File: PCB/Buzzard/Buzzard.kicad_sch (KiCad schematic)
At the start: 87 parts, among them J1 PJ-320A, J2 LCD, J4 Haptic Buzz, J5 TrackPoint, J6 OLED, J8 Battery, SW1 SW_DPST_x2, SW2 Reset, U1 ProMicro, U10 Hole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

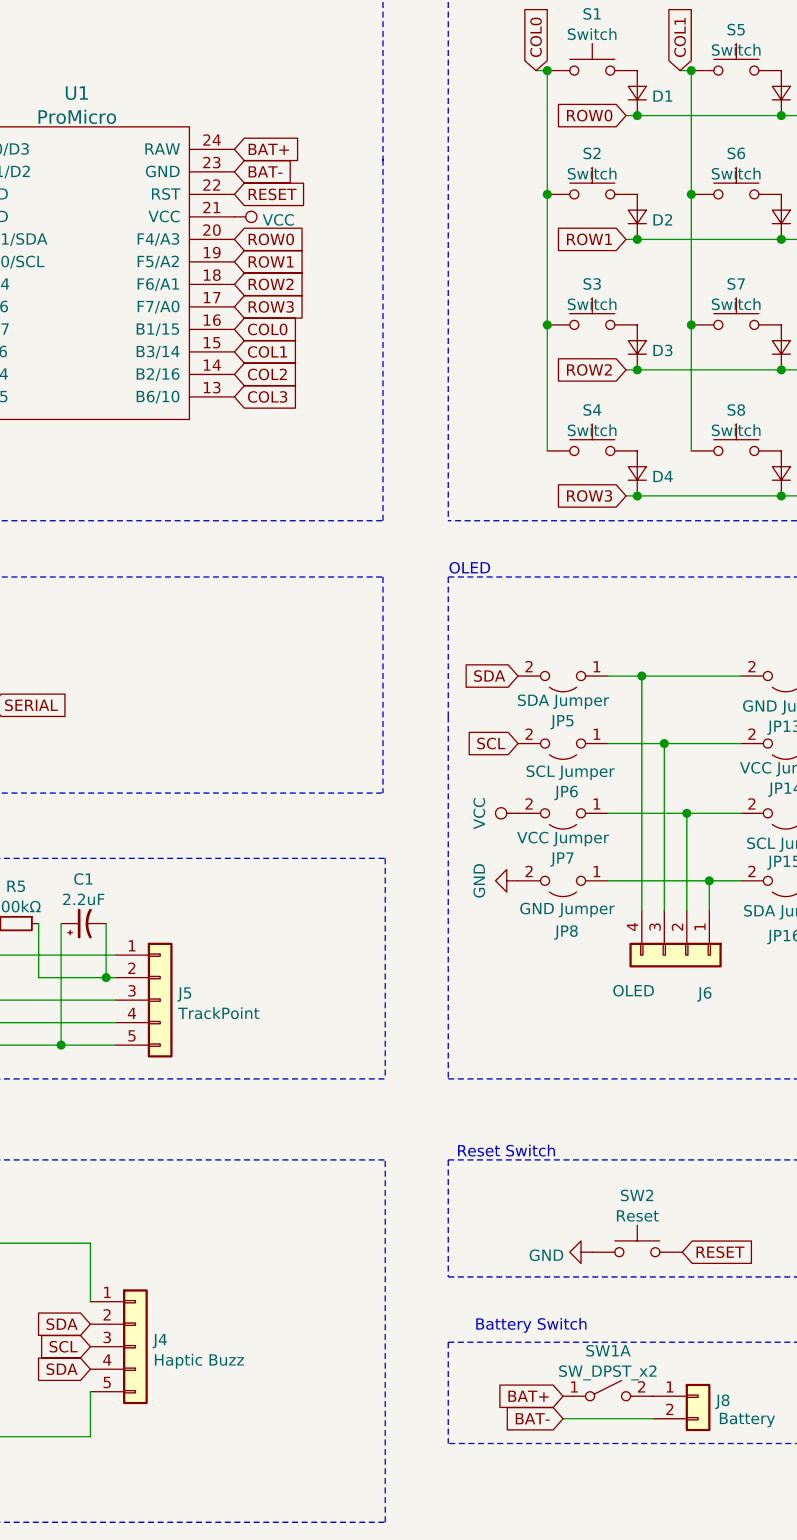
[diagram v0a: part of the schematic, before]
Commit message: rounded edge cuts
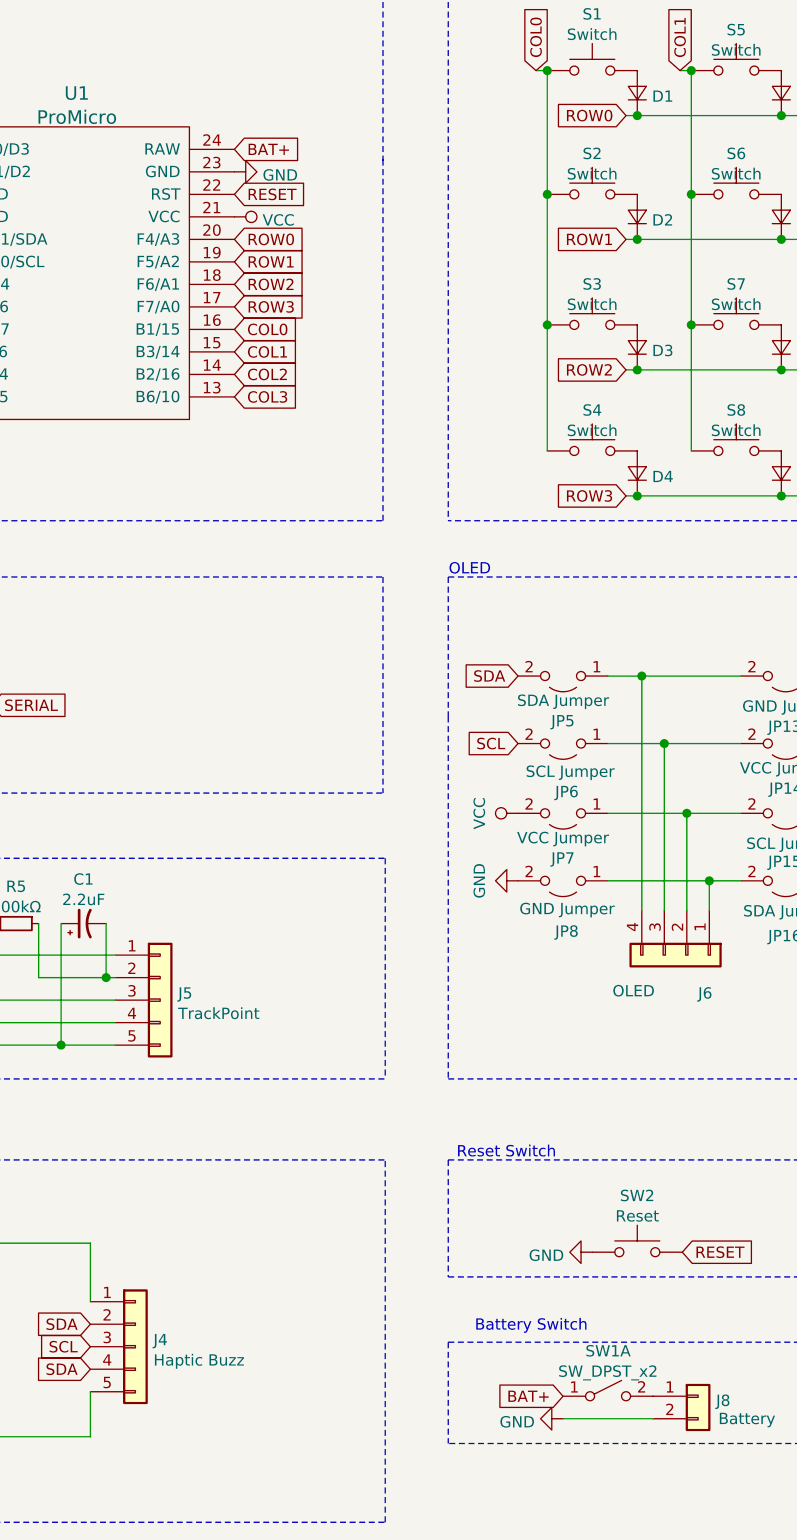
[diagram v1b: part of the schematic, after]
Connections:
- net BAT- is gone; now on net GND: J8.2 (Pin_2), U1.23 (GND)
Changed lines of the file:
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@@
-    )
-  )
-  (global_label "BAT-" (shape input) (at 89.154 37.592 0) (fields_autoplaced)
-    (effects (font (size 1.27 1.27)) (justify left))
-    (property "Intersheet References" "${INTERSHEET_REFS}" (id 0) (at 96.4657 37.6714 0)
-      (effects (font (size 1.27 1.27)) (justify left) hide)
     )
   )
@@
     )
   )
-  (global_label "BAT-" (shape input) (at 126.238 178.308 180) (fields_autoplaced)
-    (effects (font (size 1.27 1.27)) (justify right))
-    (property "Intersheet References" "${INTERSHEET_REFS}" (id 0) (at 118.9263 178.2286 0)
-      (effects (font (size 1.27 1.27)) (justify right) hide)
-    )
-  )
   (global_label "ROW0" (shape input) (at 133.35 31.242 180) (fields_autoplaced)
     (effects (font (size 1.27 1.27)) (justify right))
@@
     (pin "1")
   )
+  (symbol (lib_id "power:GND") (at 89.154 37.592 90) (unit 1)
+    (in_bom yes) (on_board yes) (fields_autoplaced)
+    (property "Reference" "#PWR?" (id 0) (at 95.504 37.592 0)
+      (effects (font (size 1.27 1.27)) hide)
+    )
+    (property "Value" "GND" (id 1) (at 92.3291 37.9805 90)
+      (effects (font (size 1.27 1.27)) (justify right))
+    )
+    (property "Footprint" "" (id 2) (at 89.154 37.592 0)
+      (effects (font (size 1.27 1.27)) hide)
+    )
+    (property "Datasheet" "" (id 3) (at 89.154 37.592 0)
+      (effects (font (size 1.27 1.27)) hide)
+    )
+    (pin "1")
+  )
   (symbol (lib_id "power:GND") (at 121.158 117.602 270) (unit 1)
     (in_bom yes) (on_board yes) (fields_autoplaced)
@@
     )
     (property "Datasheet" "" (id 3) (at 121.158 117.602 0)
+      (effects (font (size 1.27 1.27)) hide)
+    )
+    (pin "1")
+  )
+  (symbol (lib_id "power:GND") (at 126.238 178.308 270) (unit 1)
+    (in_bom yes) (on_board yes) (fields_autoplaced)
+    (property "Reference" "#PWR?" (id 0) (at 119.888 178.308 0)
+      (effects (font (size 1.27 1.27)) hide)
+    )
+    (property "Value" "GND" (id 1) (at 123.063 178.6965 90)
+      (effects (font (size 1.27 1.27)) (justify right))
+    )
+    (property "Footprint" "" (id 2) (at 126.238 178.308 0)
+      (effects (font (size 1.27 1.27)) hide)
+    )
+    (property "Datasheet" "" (id 3) (at 126.238 178.308 0)
       (effects (font (size 1.27 1.27)) hide)
     )
@@
       (reference "#PWR021") (unit 1) (value "GND") (footprint "")
     )
+    (path "/24c49c4a-95c7-4ec6-bf5c-36e77974586a"
+      (reference "#PWR?") (unit 1) (value "GND") (footprint "")
+    )
+    (path "/4907b72c-e6f0-40ff-9e41-6ac4ee21b3ef"
+      (reference "#PWR?") (unit 1) (value "GND") (footprint "")
+    )
     (path "/c869f587-3433-4e49-b864-4e64391cc97e"

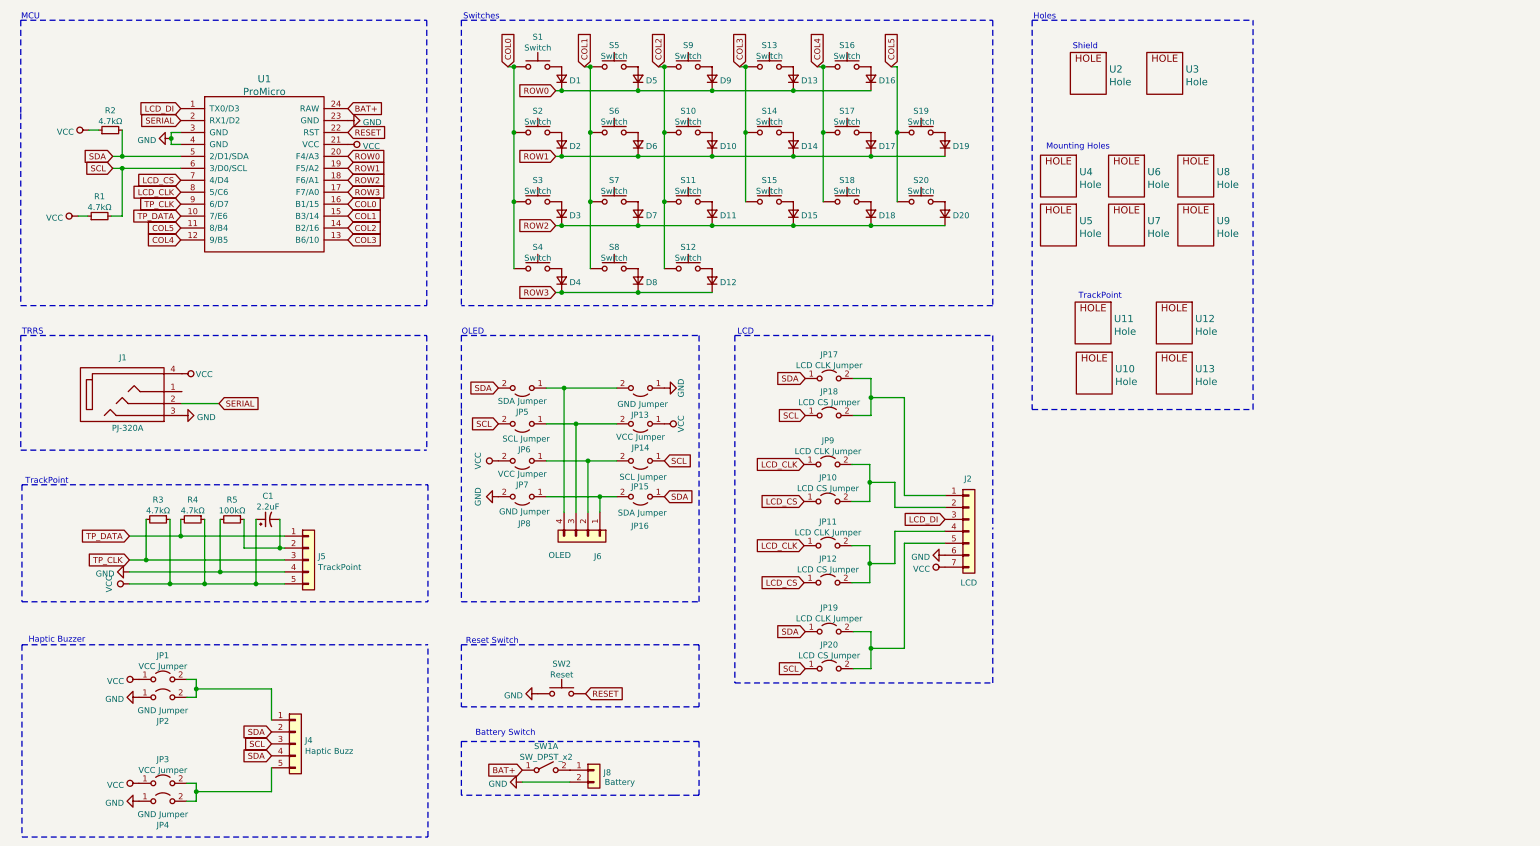
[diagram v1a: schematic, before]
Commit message: switched trrs lines and TP clock/data lines
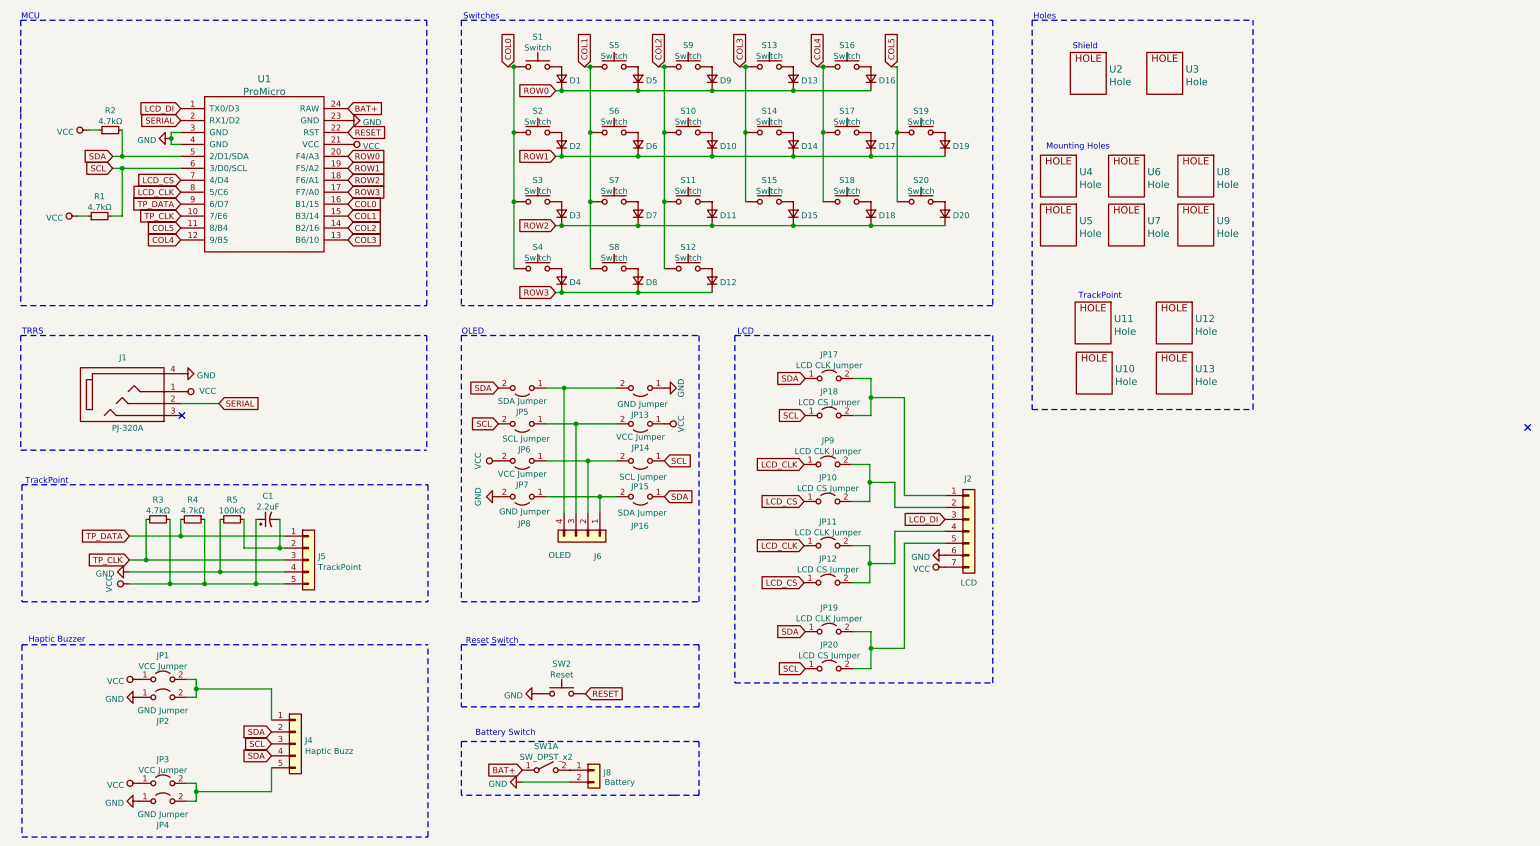
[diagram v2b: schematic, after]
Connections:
- net GND: now also J1.4; no longer J1.3
- net TP_CLK: now also U1.10 (7/E6); no longer U1.9 (6/D7)
- net TP_DATA: now also U1.9 (6/D7); no longer U1.10 (7/E6)
- net VCC: now also J1.1; no longer J1.4
- no-connect marks 0 -> 2
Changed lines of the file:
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@@
   (junction (at 200.406 149.86) (diameter 1.016) (color 0 0 0 0))
   (junction (at 205.994 40.132) (diameter 1.016) (color 0 0 0 0))
+  (no_connect (at 53.848 100.33))
+  (no_connect (at 340.106 102.87))
   (wire (pts (xy 31.75 57.912) (xy 33.782 57.912))
     (stroke (width 0) (type solid) (color 0 0 0 0))
@@
     )
   )
-  (global_label "TP_CLK" (shape input) (at 53.594 55.372 180) (fields_autoplaced)
-    (effects (font (size 1.27 1.27)) (justify right))
-    (property "Intersheet References" "${INTERSHEET_REFS}" (id 0) (at 44.4076 55.2926 0)
-      (effects (font (size 1.27 1.27)) (justify right) hide)
-    )
-  )
-  (global_label "TP_DATA" (shape input) (at 53.594 57.912 180) (fields_autoplaced)
-    (effects (font (size 1.27 1.27)) (justify right))
-    (property "Intersheet References" "${INTERSHEET_REFS}" (id 0) (at 43.5609 57.8326 0)
+  (global_label "TP_DATA" (shape input) (at 53.594 55.372 180) (fields_autoplaced)
+    (effects (font (size 1.27 1.27)) (justify right))
+    (property "Intersheet References" "${INTERSHEET_REFS}" (id 0) (at 43.5609 55.2926 0)
+      (effects (font (size 1.27 1.27)) (justify right) hide)
+    )
+  )
+  (global_label "TP_CLK" (shape input) (at 53.594 57.912 180) (fields_autoplaced)
+    (effects (font (size 1.27 1.27)) (justify right))
+    (property "Intersheet References" "${INTERSHEET_REFS}" (id 0) (at 44.4076 57.8326 0)
       (effects (font (size 1.27 1.27)) (justify right) hide)
     )
@@
     (pin "1")
   )
-  (symbol (lib_id "power:VCC") (at 53.848 91.44 270) (unit 1)
+  (symbol (lib_id "power:VCC") (at 53.848 95.25 270) (unit 1)
     (in_bom yes) (on_board yes)
-    (property "Reference" "#PWR09" (id 0) (at 50.038 91.44 0)
-      (effects (font (size 1.27 1.27)) hide)
-    )
-    (property "Value" "VCC" (id 1) (at 56.7691 91.5745 90)
+    (property "Reference" "#PWR09" (id 0) (at 50.038 95.25 0)
+      (effects (font (size 1.27 1.27)) hide)
+    )
+    (property "Value" "VCC" (id 1) (at 57.5311 95.1305 90)
       (effects (font (size 1.27 1.27)) (justify left))
     )
-    (property "Footprint" "" (id 2) (at 53.848 91.44 0)
-      (effects (font (size 1.27 1.27)) hide)
-    )
-    (property "Datasheet" "" (id 3) (at 53.848 91.44 0)
+    (property "Footprint" "" (id 2) (at 53.848 95.25 0)
+      (effects (font (size 1.27 1.27)) hide)
+    )
+    (property "Datasheet" "" (id 3) (at 53.848 95.25 0)
       (effects (font (size 1.27 1.27)) hide)
     )
@@
     (pin "1")
   )
-  (symbol (lib_id "power:GND") (at 53.848 100.33 90) (unit 1)
-    (in_bom yes) (on_board yes) (fields_autoplaced)
-    (property "Reference" "#PWR010" (id 0) (at 60.198 100.33 0)
-      (effects (font (size 1.27 1.27)) hide)
-    )
-    (property "Value" "GND" (id 1) (at 57.0231 100.7185 90)
+  (symbol (lib_id "power:GND") (at 53.848 91.44 90) (unit 1)
+    (in_bom yes) (on_board yes) (fields_autoplaced)
+    (property "Reference" "#PWR010" (id 0) (at 60.198 91.44 0)
+      (effects (font (size 1.27 1.27)) hide)
+    )
+    (property "Value" "GND" (id 1) (at 57.0231 91.8285 90)
       (effects (font (size 1.27 1.27)) (justify right))
     )
-    (property "Footprint" "" (id 2) (at 53.848 100.33 0)
-      (effects (font (size 1.27 1.27)) hide)
-    )
-    (property "Datasheet" "" (id 3) (at 53.848 100.33 0)
-      (effects (font (size 1.27 1.27)) hide)
-    )
+    (property "Footprint" "" (id 2) (at 53.848 91.44 0)
+      (effects (font (size 1.27 1.27)) hide)
+    )
+    (property "Datasheet" "" (id 3) (at 53.848 91.44 0)
+      (effects (font (size 1.27 1.27)) hide)
+    )

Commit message: Some fine tuning and silkmask improvments
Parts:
- JP17, JP19: value LCD CLK Jumper -> LCD EIN Jumper
- JP18, JP20: value LCD CS Jumper -> LCD DISP Jumper
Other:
- title: (none) -> Buzzard Split Keyboard
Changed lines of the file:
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@@
 (kicad_sch (version 20210406) (generator eeschema)
   (paper "A4")
+  (title_block
+    (title "Buzzard Split Keyboard")
+    (date "2021-11-13")
+    (rev "1")
+  )
   (junction (at 41.148 45.212) (diameter 1.016) (color 0 0 0 0))
   (junction (at 41.148 47.752) (diameter 1.016) (color 0 0 0 0))
@@
     (in_bom yes) (on_board yes) (fields_autoplaced)
     (property "Reference" "JP17" (id 0) (at 191.516 87.3718 0))
-    (property "Value" "LCD CLK Jumper" (id 1) (at 191.516 89.6705 0))
+    (property "Value" "LCD EIN Jumper" (id 1) (at 191.516 89.6705 0))
     (property "Footprint" "Jumper:SolderJumper-2_P1.3mm_Open_Pad1.0x1.5mm" (id 2) (at 191.516 92.456 0)
       (effects (font (size 1.27 1.27)) hide)
@@
     (in_bom yes) (on_board yes) (fields_autoplaced)
     (property "Reference" "JP18" (id 0) (at 191.516 95.2458 0))
-    (property "Value" "LCD CS Jumper" (id 1) (at 191.516 97.5445 0))
+    (property "Value" "LCD DISP Jumper" (id 1) (at 191.516 97.5445 0))
     (property "Footprint" "Jumper:SolderJumper-2_P1.3mm_Open_Pad1.0x1.5mm" (id 2) (at 191.516 100.33 0)
       (effects (font (size 1.27 1.27)) hide)
@@
     (in_bom yes) (on_board yes) (fields_autoplaced)
     (property "Reference" "JP19" (id 0) (at 191.516 141.2198 0))
-    (property "Value" "LCD CLK Jumper" (id 1) (at 191.516 143.5185 0))
+    (property "Value" "LCD EIN Jumper" (id 1) (at 191.516 143.5185 0))
     (property "Footprint" "Jumper:SolderJumper-2_P1.3mm_Open_Pad1.0x1.5mm" (id 2) (at 191.516 146.304 0)
       (effects (font (size 1.27 1.27)) hide)
@@
     (in_bom yes) (on_board yes) (fields_autoplaced)
     (property "Reference" "JP20" (id 0) (at 191.516 149.0938 0))
-    (property "Value" "LCD CS Jumper" (id 1) (at 191.516 151.3925 0))
+    (property "Value" "LCD DISP Jumper" (id 1) (at 191.516 151.3925 0))
     (property "Footprint" "Jumper:SolderJumper-2_P1.3mm_Open_Pad1.0x1.5mm" (id 2) (at 191.516 154.178 0)
       (effects (font (size 1.27 1.27)) hide)
@@
     )
     (path "/e7932f86-c33d-462c-8de4-76ea75a5e908"
-      (reference "JP17") (unit 1) (value "LCD CLK Jumper") (footprint "Jumper:SolderJumper-2_P1.3mm_Open_Pad1.0x1.5mm")
+      (reference "JP17") (unit 1) (value "LCD EIN Jumper") (footprint "Jumper:SolderJumper-2_P1.3mm_Open_Pad1.0x1.5mm")
     )
     (path "/62c268eb-d4cf-42e9-a63f-1492f947d6e7"
-      (reference "JP18") (unit 1) (value "LCD CS Jumper") (footprint "Jumper:SolderJumper-2_P1.3mm_Open_Pad1.0x1.5mm")
+      (reference "JP18") (unit 1) (value "LCD DISP Jumper") (footprint "Jumper:SolderJumper-2_P1.3mm_Open_Pad1.0x1.5mm")
     )
     (path "/b2081f34-5deb-486f-996a-ccef8d60faf4"
-      (reference "JP19") (unit 1) (value "LCD CLK Jumper") (footprint "Jumper:SolderJumper-2_P1.3mm_Open_Pad1.0x1.5mm")
+      (reference "JP19") (unit 1) (value "LCD EIN Jumper") (footprint "Jumper:SolderJumper-2_P1.3mm_Open_Pad1.0x1.5mm")
     )
     (path "/bfad2d1f-46da-4d69-9f17-d22bc1bd4fe6"
-      (reference "JP20") (unit 1) (value "LCD CS Jumper") (footprint "Jumper:SolderJumper-2_P1.3mm_Open_Pad1.0x1.5mm")
+      (reference "JP20") (unit 1) (value "LCD DISP Jumper") (footprint "Jumper:SolderJumper-2_P1.3mm_Open_Pad1.0x1.5mm")
     )
     (path "/48543692-40e8-46fb-b05c-77cf9495e218"
